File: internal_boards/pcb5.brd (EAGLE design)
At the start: 100 x 80 mm, 8 parts, among them IC1 LM555N

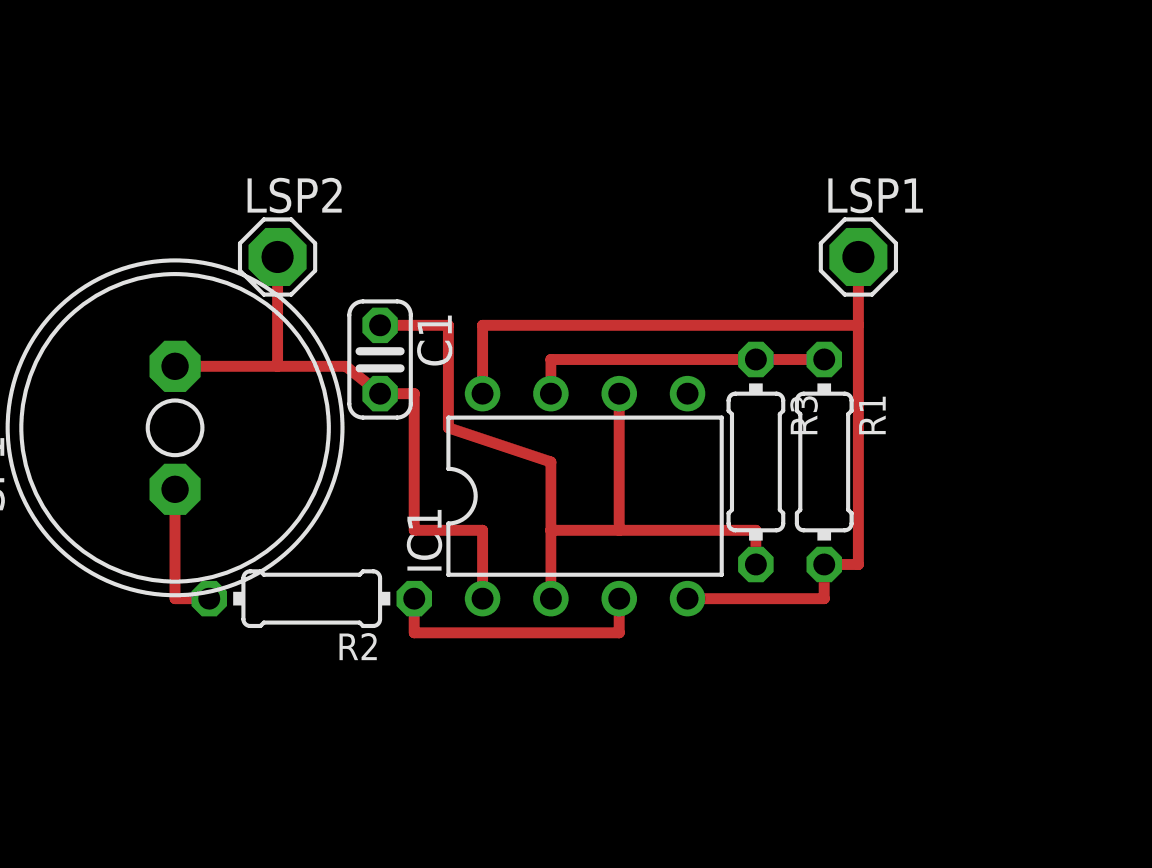
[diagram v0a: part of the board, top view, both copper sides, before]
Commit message: * Adding in jumper for on/off
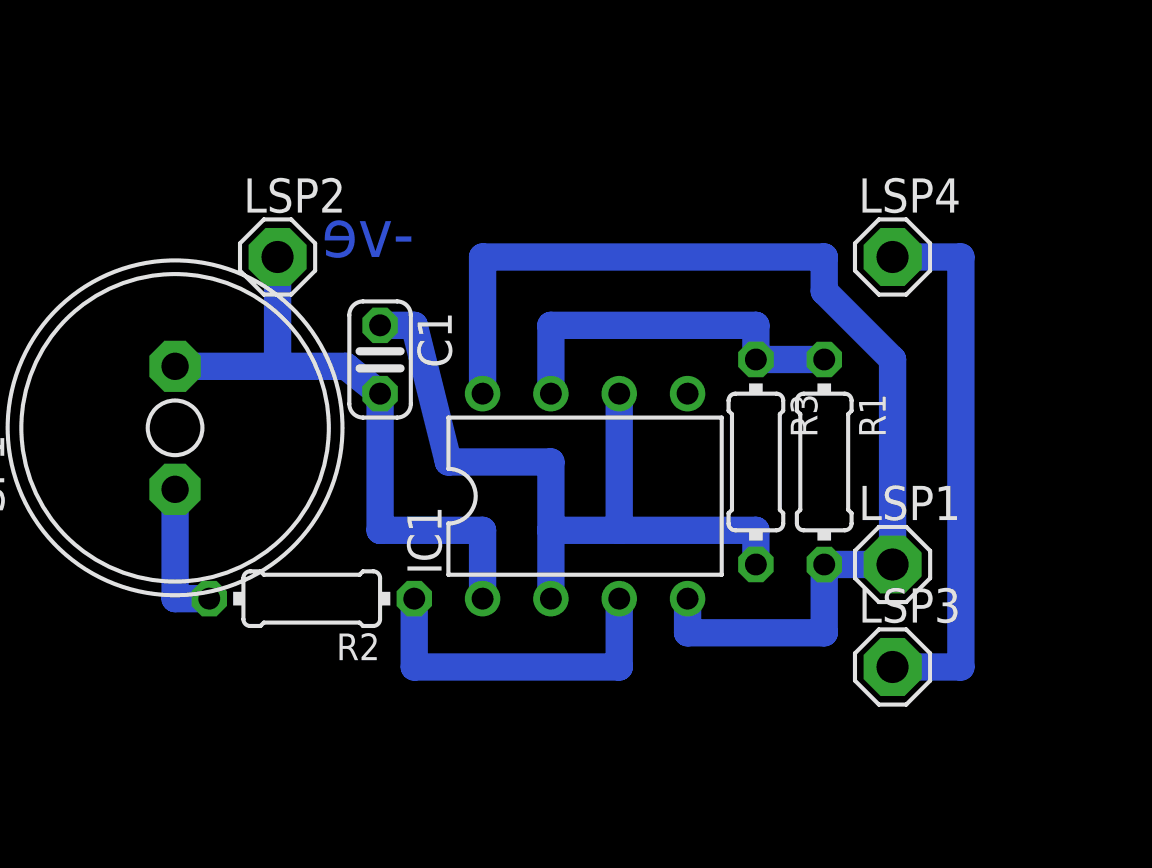
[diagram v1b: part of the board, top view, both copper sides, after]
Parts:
- added LSP3, LSP4: MCS08, solpad:MCS08
- moved LSP1 11.5 mm to (53.3, 30.5)
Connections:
- new net N$7: IC1.4, IC1.8, LSP1.MP, R1.2
- net VCC: now also LSP3.MP, LSP4.MP; no longer IC1.4, IC1.8, LSP1.MP, R1.2
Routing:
- net N$7: track 0.00 -> 41.7 mm
- net VCC: track 35.6 -> 20.3 mm
- net N$1: track 10.2 -> 12.7 mm
- net N$2: track 11.4 -> 14.0 mm
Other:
- board text added: "-ve"
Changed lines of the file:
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@@
 <wire x1="100" y1="80" x2="0" y2="80" width="0" layer="20"/>
 <wire x1="0" y1="80" x2="0" y2="0" width="0" layer="20"/>
+<text x="35.56" y="41.91" size="1.778" layer="16" rot="MR0">-ve</text>
 </plain>
 <attributes>
@@
 <attribute name="OC_FARNELL" value="unknown" x="26.67" y="35.56" size="1.778" layer="27" rot="R90" display="off"/>
 </element>
-<element name="LSP1" library="solpad" package="MCS08" value="MCS08" x="52.07" y="41.91"/>
+<element name="LSP1" library="solpad" package="MCS08" value="MCS08" x="53.34" y="30.48"/>
 <element name="LSP2" library="solpad" package="MCS08" value="MCS08" x="30.48" y="41.91"/>
+<element name="LSP3" library="solpad" package="MCS08" value="MCS08" x="53.34" y="26.67"/>
+<element name="LSP4" library="solpad" package="MCS08" value="MCS08" x="53.34" y="41.91"/>
 </elements>
 <signals>
@@
 <contactref element="IC1" pad="3"/>
 <contactref element="R2" pad="1"/>
-<wire x1="35.56" y1="29.21" x2="35.56" y2="27.94" width="0.4064" layer="1"/>
-<wire x1="35.56" y1="27.94" x2="43.18" y2="27.94" width="0.4064" layer="1"/>
-<wire x1="43.18" y1="27.94" x2="43.18" y2="29.21" width="0.4064" layer="1"/>
+<wire x1="35.56" y1="29.21" x2="35.56" y2="26.67" width="1.016" layer="16"/>
+<wire x1="35.56" y1="26.67" x2="43.18" y2="26.67" width="1.016" layer="16"/>
+<wire x1="43.18" y1="26.67" x2="43.18" y2="29.21" width="1.016" layer="16"/>
 </signal>
 <signal name="N$2">
@@
 <contactref element="R1" pad="1"/>
 <contactref element="R3" pad="1"/>
-<wire x1="50.8" y1="38.1" x2="48.26" y2="38.1" width="0.4064" layer="1"/>
-<wire x1="48.26" y1="38.1" x2="40.64" y2="38.1" width="0.4064" layer="1"/>
-<wire x1="40.64" y1="38.1" x2="40.64" y2="36.83" width="0.4064" layer="1"/>
+<wire x1="50.8" y1="38.1" x2="48.26" y2="38.1" width="1.016" layer="16"/>
+<wire x1="48.26" y1="38.1" x2="48.26" y2="39.37" width="1.016" layer="16"/>
+<wire x1="48.26" y1="39.37" x2="40.64" y2="39.37" width="1.016" layer="16"/>
+<wire x1="40.64" y1="39.37" x2="40.64" y2="36.83" width="1.016" layer="16"/>
 </signal>
 <signal name="N$4">
@@
 <contactref element="C1" pad="1"/>
 <contactref element="R3" pad="2"/>
-<wire x1="43.18" y1="36.83" x2="43.18" y2="31.75" width="0.4064" layer="1"/>
-<wire x1="43.18" y1="31.75" x2="48.26" y2="31.75" width="0.4064" layer="1"/>
-<wire x1="48.26" y1="31.75" x2="48.26" y2="30.48" width="0.4064" layer="1"/>
-<wire x1="40.64" y1="29.21" x2="40.64" y2="31.75" width="0.4064" layer="1"/>
-<wire x1="40.64" y1="31.75" x2="43.18" y2="31.75" width="0.4064" layer="1"/>
-<wire x1="34.29" y1="39.37" x2="36.83" y2="39.37" width="0.4064" layer="1"/>
-<wire x1="36.83" y1="39.37" x2="36.83" y2="35.56" width="0.4064" layer="1"/>
-<wire x1="36.83" y1="35.56" x2="40.64" y2="34.29" width="0.4064" layer="1"/>
-<wire x1="40.64" y1="34.29" x2="40.64" y2="31.75" width="0.4064" layer="1"/>
+<wire x1="43.18" y1="36.83" x2="43.18" y2="31.75" width="1.016" layer="16"/>
+<wire x1="43.18" y1="31.75" x2="48.26" y2="31.75" width="1.016" layer="16"/>
+<wire x1="48.26" y1="31.75" x2="48.26" y2="30.48" width="1.016" layer="16"/>
+<wire x1="40.64" y1="29.21" x2="40.64" y2="31.75" width="1.016" layer="16"/>
+<wire x1="40.64" y1="31.75" x2="43.18" y2="31.75" width="1.016" layer="16"/>
+<wire x1="34.29" y1="39.37" x2="35.56" y2="39.37" width="1.016" layer="16"/>
+<wire x1="35.56" y1="39.37" x2="36.83" y2="34.29" width="1.016" layer="16"/>
+<wire x1="36.83" y1="34.29" x2="40.64" y2="34.29" width="1.016" layer="16"/>
+<wire x1="40.64" y1="34.29" x2="40.64" y2="31.75" width="1.016" layer="16"/>
 </signal>
 <signal name="GND">
@@
 <contactref element="C1" pad="2"/>
 <contactref element="SP1" pad="+"/>
-<wire x1="34.29" y1="36.83" x2="35.56" y2="36.83" width="0.4064" layer="1"/>
-<wire x1="35.56" y1="36.83" x2="35.56" y2="31.75" width="0.4064" layer="1"/>
-<wire x1="35.56" y1="31.75" x2="38.1" y2="31.75" width="0.4064" layer="1"/>
-<wire x1="38.1" y1="31.75" x2="38.1" y2="29.21" width="0.4064" layer="1"/>
-<wire x1="26.67" y1="37.846" x2="30.48" y2="37.846" width="0.4064" layer="1"/>
-<wire x1="30.48" y1="37.846" x2="33.02" y2="37.846" width="0.4064" layer="1"/>
-<wire x1="33.02" y1="37.846" x2="34.29" y2="36.83" width="0.4064" layer="1"/>
+<wire x1="34.29" y1="36.83" x2="34.29" y2="31.75" width="1.016" layer="16"/>
+<wire x1="34.29" y1="31.75" x2="38.1" y2="31.75" width="1.016" layer="16"/>
+<wire x1="38.1" y1="31.75" x2="38.1" y2="29.21" width="1.016" layer="16"/>
+<wire x1="26.67" y1="37.846" x2="30.48" y2="37.846" width="1.016" layer="16"/>
+<wire x1="30.48" y1="37.846" x2="33.02" y2="37.846" width="1.016" layer="16"/>
+<wire x1="33.02" y1="37.846" x2="34.29" y2="36.83" width="1.016" layer="16"/>
 <contactref element="LSP2" pad="MP"/>
-<wire x1="30.48" y1="41.91" x2="30.48" y2="37.846" width="0.4064" layer="1"/>
-</signal>
-<signal name="VCC">
-<contactref element="IC1" pad="4"/>
-<contactref element="IC1" pad="8"/>
-<contactref element="R1" pad="2"/>
-<wire x1="50.8" y1="30.48" x2="50.8" y2="29.21" width="0.4064" layer="1"/>
-<wire x1="50.8" y1="29.21" x2="45.72" y2="29.21" width="0.4064" layer="1"/>
-<wire x1="38.1" y1="36.83" x2="38.1" y2="39.37" width="0.4064" layer="1"/>
-<wire x1="38.1" y1="39.37" x2="52.07" y2="39.37" width="0.4064" layer="1"/>
-<wire x1="52.07" y1="39.37" x2="52.07" y2="30.48" width="0.4064" layer="1"/>
-<wire x1="52.07" y1="30.48" x2="50.8" y2="30.48" width="0.4064" layer="1"/>
-<wire x1="52.07" y1="39.37" x2="52.07" y2="41.91" width="0.4064" layer="1"/>
-<contactref element="LSP1" pad="MP"/>
-<wire x1="52.07" y1="41.91" x2="52.07" y2="41.91" width="0" layer="19" extent="1-1"/>
+<wire x1="30.48" y1="41.91" x2="30.48" y2="37.846" width="1.016" layer="16"/>
 </signal>
 <signal name="N$3">
 <contactref element="SP1" pad="-"/>
 <contactref element="R2" pad="2"/>
-<wire x1="27.94" y1="29.21" x2="26.67" y2="29.21" width="0.4064" layer="1"/>
-<wire x1="26.67" y1="29.21" x2="26.67" y2="33.274" width="0.4064" layer="1"/>
+<wire x1="27.94" y1="29.21" x2="26.67" y2="29.21" width="1.016" layer="16"/>
+<wire x1="26.67" y1="29.21" x2="26.67" y2="33.274" width="1.016" layer="16"/>
 </signal>
 <signal name="N$5">
 </signal>
+<signal name="N$7">
+<contactref element="IC1" pad="4"/>
+<contactref element="LSP1" pad="MP"/>
+<contactref element="IC1" pad="8"/>
+<contactref element="R1" pad="2"/>
+<wire x1="38.1" y1="36.83" x2="38.1" y2="41.91" width="1.016" layer="16"/>
+<wire x1="53.34" y1="30.48" x2="50.8" y2="30.48" width="1.016" layer="16"/>
+<wire x1="45.72" y1="29.21" x2="45.72" y2="27.94" width="1.016" layer="16"/>
+<wire x1="45.72" y1="27.94" x2="50.8" y2="27.94" width="1.016" layer="16"/>
+<wire x1="50.8" y1="27.94" x2="50.8" y2="30.48" width="1.016" layer="16"/>
+<wire x1="38.1" y1="41.91" x2="50.8" y2="41.91" width="1.016" layer="16"/>
+<wire x1="50.8" y1="40.64" x2="53.34" y2="38.1" width="1.016" layer="16"/>
+<wire x1="50.8" y1="41.91" x2="50.8" y2="40.64" width="1.016" layer="16"/>
+<wire x1="53.34" y1="30.48" x2="53.34" y2="38.1" width="1.016" layer="16"/>
+<wire x1="53.34" y1="38.1" x2="50.8" y2="40.64" width="0" layer="19" extent="1-16"/>
+</signal>
+<signal name="VCC">
+<contactref element="LSP3" pad="MP"/>
+<contactref element="LSP4" pad="MP"/>
+<wire x1="53.34" y1="26.67" x2="55.88" y2="26.67" width="1.016" layer="16"/>
+<wire x1="55.88" y1="26.67" x2="55.88" y2="41.91" width="1.016" layer="16"/>
+<wire x1="55.88" y1="41.91" x2="53.34" y2="41.91" width="1.016" layer="16"/>
+</signal>
 </signals>
